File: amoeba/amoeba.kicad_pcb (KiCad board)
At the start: 2 copper layers, 18.8 x 16.1 mm, 23 parts

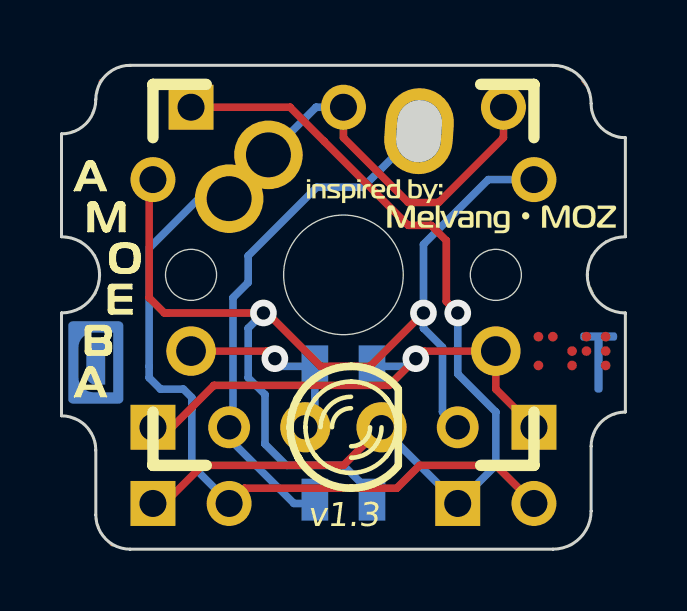
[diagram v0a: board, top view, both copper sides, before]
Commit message: Updates to amoeba 1u and 2u.
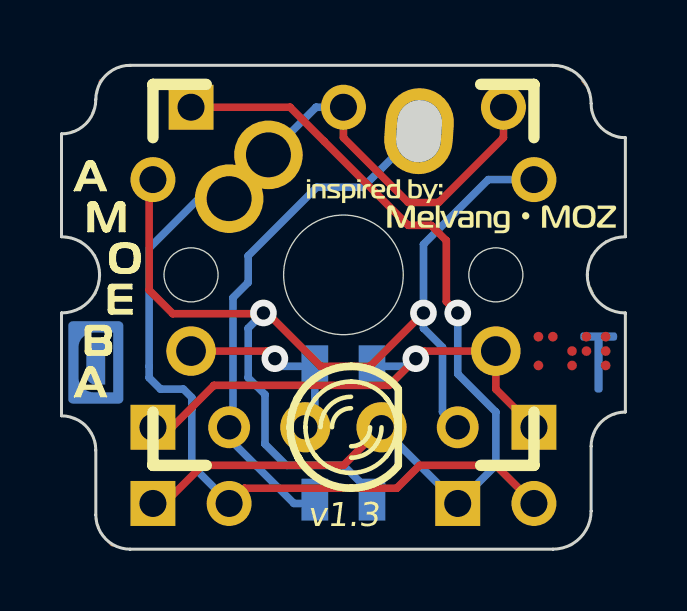
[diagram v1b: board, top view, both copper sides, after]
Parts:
- S0: footprint ALPS_CHERRY_PCB_100H -> ALPS_CHERRY_ZEAL_PCB_100H

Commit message: Added pad arrows.
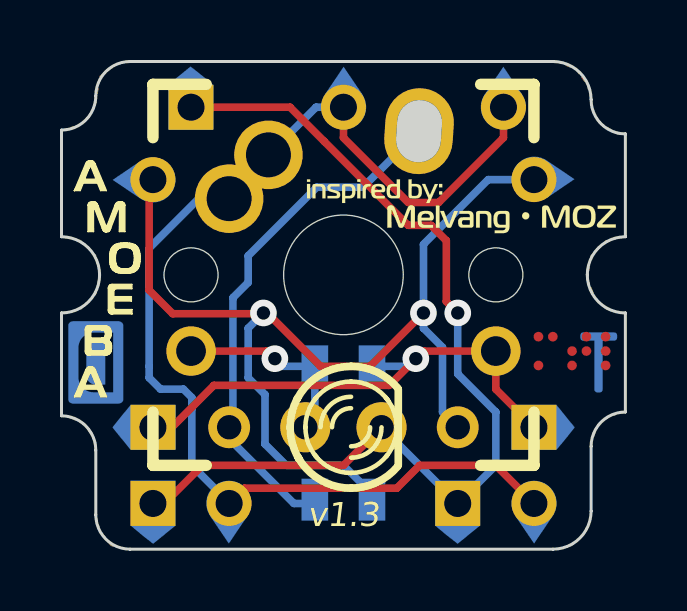
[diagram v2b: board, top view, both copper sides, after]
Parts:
- added pad-arrow-round: G***, pad-arrow-round, B.Cu at (255.6, 107.3)
- added pad-arrow-round: G***, pad-arrow-round, B.Cu at (242.3, 107.3)
- added pad-arrow-round: G***, pad-arrow-round, B.Cu at (254.2, 104.6)
- added pad-arrow-round: G***, pad-arrow-round, B.Cu at (248.9, 104.6)
- added pad-arrow-round: G***, pad-arrow-round, B.Cu at (255.3, 118.4)
- added pad-arrow-round: G***, pad-arrow-round, B.Cu at (245.1, 118.4)
- added pad-arrow-square: G***, pad-arrow-square, B.Cu at (255.6, 115.6)
- added pad-arrow-square: G***, pad-arrow-square, B.Cu at (242.3, 115.6)
- added pad-arrow-square: G***, pad-arrow-square, B.Cu at (243.8, 104.6)
- added pad-arrow-square: G***, pad-arrow-square, B.Cu at (242.6, 118.4)
- added pad-arrow-square: G***, pad-arrow-square, B.Cu at (252.7, 118.4)
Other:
- board size 18.8 x 16.1 mm -> 18.8 x 16.3 mm

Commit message: Fix oversized mask on pad arrows.
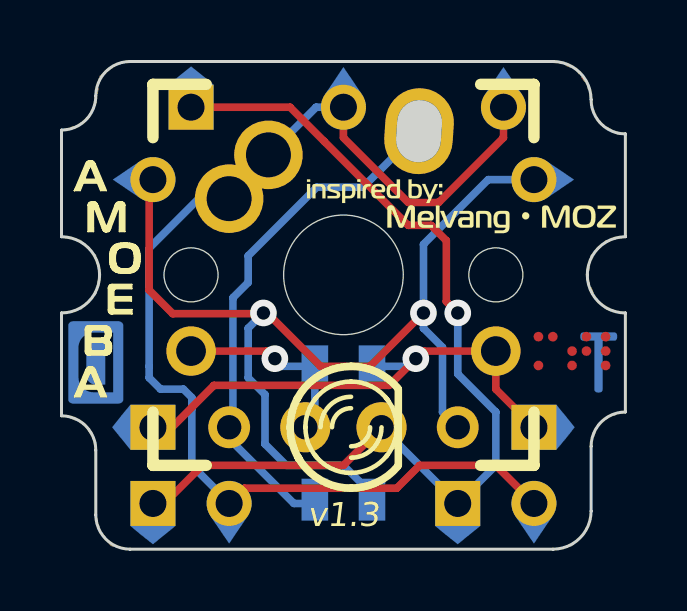
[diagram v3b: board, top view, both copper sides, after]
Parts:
- removed the pad-arrow-round at (255.6, 107.3)
- removed the pad-arrow-round at (242.3, 107.3)
- removed the pad-arrow-round at (254.2, 104.6)
- removed the pad-arrow-round at (248.9, 104.6)
- removed the pad-arrow-round at (255.3, 118.4)
- removed the pad-arrow-round at (245.1, 118.4)
- removed the pad-arrow-square at (255.6, 115.6)
- removed the pad-arrow-square at (242.3, 115.6)
- removed the pad-arrow-square at (243.8, 104.6)
- removed the pad-arrow-square at (242.6, 118.4)
- removed the pad-arrow-square at (252.7, 118.4)
- added pad-arrow-round: G***, pad-arrow-round, B.Cu at (254.3, 104.6)
- added pad-arrow-round: G***, pad-arrow-round, B.Cu at (248.9, 104.6)
- added pad-arrow-round: G***, pad-arrow-round, B.Cu at (242.3, 107.3)
- added pad-arrow-round: G***, pad-arrow-round, B.Cu at (245.1, 118.4)
- added pad-arrow-round: G***, pad-arrow-round, B.Cu at (255.3, 118.4)
- added pad-arrow-round: G***, pad-arrow-round, B.Cu at (255.6, 107.3)
- added pad-arrow-square: G***, pad-arrow-square, B.Cu at (243.8, 104.6)
- added pad-arrow-square: G***, pad-arrow-square, B.Cu at (242.3, 115.6)
- added pad-arrow-square: G***, pad-arrow-square, B.Cu at (242.6, 118.4)
- added pad-arrow-square: G***, pad-arrow-square, B.Cu at (252.7, 118.4)
- added pad-arrow-square: G***, pad-arrow-square, B.Cu at (255.6, 115.6)

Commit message: Tighten solder masks, add pad arrows to amoeba-stabilizer-2, convert amoeba on 2u to copper.
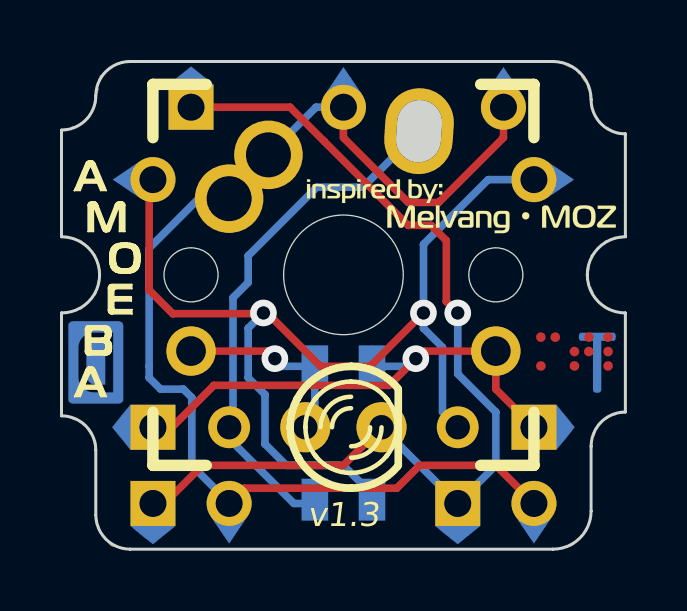
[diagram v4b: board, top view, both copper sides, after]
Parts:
- moved dt-logo-t-rev 0.06 mm to (257.4, 113.3)
- moved mtl-braille 0.06 mm to (256.5, 113.0)

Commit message: Update to version 1.5.
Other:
- board text added: "v1.5"
- board text removed: "v1.3"
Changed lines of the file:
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@@
     (21 F.SilkS user)
     (22 B.Mask user hide)
-    (23 F.Mask user)
+    (23 F.Mask user hide)
     (24 Dwgs.User user hide)
     (25 Cmts.User user hide)
@@
   (gr_arc (start 239.522 116.332) (end 239.522 115.189) (angle 90) (layer Edge.Cuts) (width 0.1))
   (gr_line (start 240.665 116.332) (end 240.665 118.491) (angle 90) (layer Edge.Cuts) (width 0.1))
-  (gr_text v1.3 (at 257.175 107.061 90) (layer B.SilkS)
+  (gr_text v1.5 (at 257.175 107.061 90) (layer B.SilkS)
     (effects (font (size 0.8 0.8) (thickness 0.15) italic) (justify mirror))
   )
-  (gr_text v1.3 (at 248.92 118.491) (layer F.SilkS)
+  (gr_text v1.5 (at 248.92 118.491) (layer F.SilkS)
     (effects (font (size 0.8 0.8) (thickness 0.12) italic))
   )
